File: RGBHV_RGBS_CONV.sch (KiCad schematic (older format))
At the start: 29 parts, among them J1 DIGITAL RGB, J10 ENABLE_DIVIDE, J11 RGBHV_1, J12 LOGIC_SINGLE, J13 LOGIC_DOUBLE, J14 ENABLE_MARGE, J15 RGBS_OUT, J16 RGBS_OUT, J17 +5V IN, J18 +5V OUT, J2 VGA DB15, J3 ANALOG RGB DB15, J4 X1, J5 DIGITAL_RGBHV_1, J6 ANALOG RGB, J7 DIGITAL_RGBHV_2, J8 ANALOG RGB VGA, J9 RGBHV_1, U1 LM1881, U2 74HC86

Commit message: Rev.5A DIn8 fix and remove sync sep.
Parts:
- removed C1: C, Capacitors_ThroughHole:C_Disc_D4.3mm_W1.9mm_P5.00mm, symbol Device:C
- removed C3, C4: C, Capacitors_ThroughHole:C_Disc_D4.3mm_W1.9mm_P5.00mm, symbol device:C
- removed J10: ENABLE_DIVIDE, Pin_Headers:Pin_Header_Straight_1x02_Pitch2.54mm, symbol Connector_Generic:Conn_01x02
- removed J12: LOGIC_SINGLE, Pin_Headers:Pin_Header_Straight_1x02_Pitch2.54mm, symbol Connector_Generic:Conn_01x02
- removed J13: LOGIC_DOUBLE, Pin_Headers:Pin_Header_Straight_1x02_Pitch2.54mm, symbol Connector_Generic:Conn_01x02
- removed J14: ENABLE_MARGE, Pin_Headers:Pin_Header_Straight_1x02_Pitch2.54mm, symbol Connector_Generic:Conn_01x02
- removed J8: ANALOG RGB VGA, Pin_Headers:Pin_Header_Straight_2x08_Pitch2.54mm, symbol Connector_Generic:Conn_02x08_Top_Bottom
- removed R4: R, Resistors_ThroughHole:R_Axial_DIN0204_L3.6mm_D1.6mm_P5.08mm_Horizontal, symbol Device:R
- removed RV1: R_POT, Potentiometers:Potentiometer_Triwood_RM-065, symbol Device:R_POT
- removed U1: LM1881, Housings_DIP:DIP-8_W7.62mm, symbol Video:LM1881
- removed U2: 74HC86, Housings_DIP:DIP-14_W7.62mm, symbol ryuk_org:74HC86
- added J8: ANALOG RGB DA15 EDGE, ryuk_lib:D-SUB15_PCB_EDGE, symbol Connector:DB15_Female_MountingHoles
- added U2: 4070/74HC86, symbol ryuk_lib:74HC86-ryuk_org-RGBHV_RGBS_CONV-rescue-RGBHV_RGBS_CONV-rescue
- J3: value ANALOG RGB DB15 -> ANALOG RGB DA15
- R1, R2, R3: footprint Resistors_ThroughHole:R_Axial_DIN0204_L3.6mm_D1.6mm_P5.08mm_Horizontal -> Resistor_THT:R_Axial_DIN0204_L3.6mm_D1.6mm_P7.62mm_Horizontal
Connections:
- wire segments 172 -> 138
- no-connect marks 44 -> 49
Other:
- moved on the sheet: C2, J1, J11, J15, J16, J17, J18, J2, J3, J4, J5, J6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

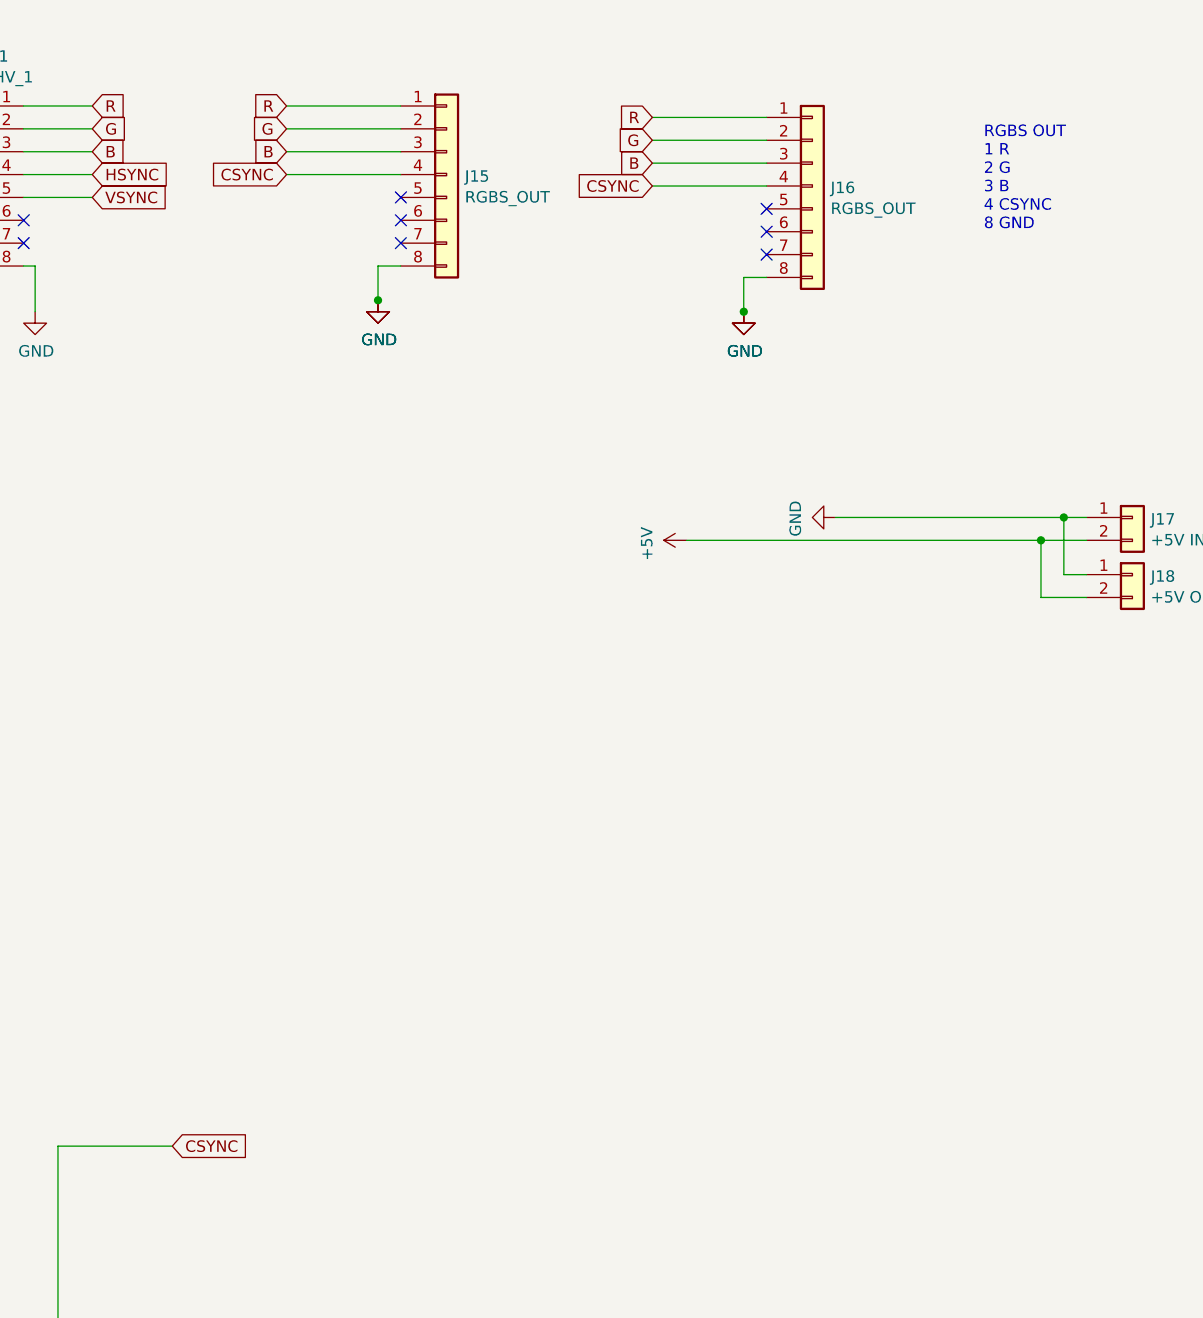
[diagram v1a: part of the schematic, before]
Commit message: Rev.5B Add RGBS VR
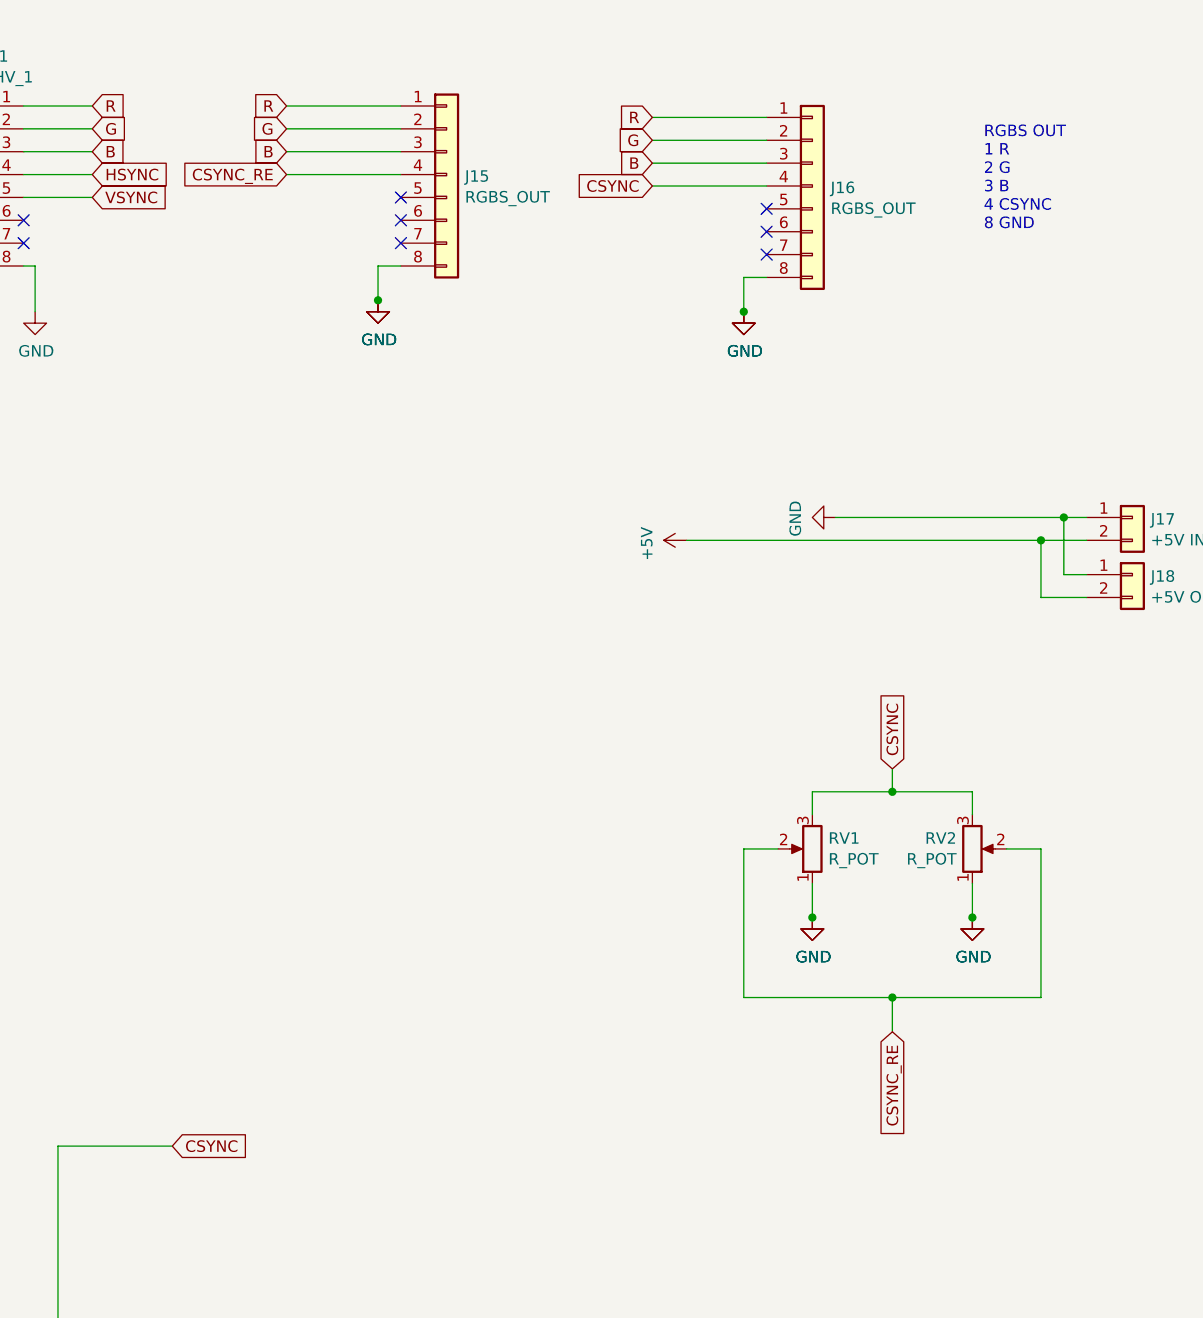
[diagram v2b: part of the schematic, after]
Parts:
- added RV1, RV2: R_POT, Potentiometer_THT:Potentiometer_Bourns_3296W_Vertical, symbol Device:R_POT
- U2: footprint (none) -> Package_DIP:DIP-14_W7.62mm
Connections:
- net CSYNC: now also RV1.3, RV2.3; no longer J15.4 (Pin_4)
- net GND: now also RV1.1, RV2.1
- new net CSYNC_RE: J15.4 (Pin_4), RV1.2, RV2.2
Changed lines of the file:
@@
 	14250 3550 15250 3550
 Text GLabel 11850 2050 0    50   Input ~ 0
-CSYNC
+CSYNC_RE
 $Comp
 L power:GND #PWR026
@@
 Wire Wire Line
 	2050 5150 2950 5150
+NoConn ~ 6700 2250
+NoConn ~ 6700 2350
+NoConn ~ 9750 2250
+NoConn ~ 9750 2350
+NoConn ~ 10700 2250
+NoConn ~ 10700 2350
+Wire Wire Line
+	10850 6300 10850 8200
+Wire Wire Line
+	9700 8200 10850 8200
+Wire Wire Line
+	10150 8400 12050 8400
+$Comp
+L power:GND #PWR012
+U 1 1 5D43FAA1
+P 6100 5650
+F 0 "#PWR012" H 6100 5400 50  0001 C CNN
+F 1 "GND" H 6105 5477 50  0000 C CNN
+F 2 "" H 6100 5650 50  0001 C CNN
+F 3 "" H 6100 5650 50  0001 C CNN
+	1    6100 5650
+	1    0    0    -1
+$EndComp
+Wire Wire Line
+	6100 5450 6100 5650
+Wire Wire Line
+	5800 3850 5050 3850
+Wire Wire Line
+	4950 4250 5800 4250
+Wire Wire Line
+	5800 4650 4850 4650
+Wire Wire Line
+	5800 4050 5400 4050
+Wire Wire Line
+	5400 4050 5400 4450
+Wire Wire Line
+	5400 4450 5800 4450
+Wire Wire Line
+	5400 4850 5800 4850
+Connection ~ 5400 4450
+Connection ~ 5400 4850
+$Comp
+L power:GND #PWR010
+U 1 1 5D43FAB5
+P 5400 5450
+F 0 "#PWR010" H 5400 5200 50  0001 C CNN
+F 1 "GND" H 5405 5277 50  0000 C CNN
+F 2 "" H 5400 5450 50  0001 C CNN
+F 3 "" H 5400 5450 50  0001 C CNN
+	1    5400 5450
+	1    0    0    -1
+$EndComp
+NoConn ~ 5800 3950
+NoConn ~ 5800 4150
+NoConn ~ 5800 4350
+NoConn ~ 5800 4750
+NoConn ~ 5800 5050
+Wire Wire Line
+	5400 4850 5400 5450
+NoConn ~ 5800 5250
+Wire Wire Line
+	5400 4450 5400 4850
+NoConn ~ 5800 4550
+Text GLabel 4900 4950 0    50   Input ~ 0
+HSYNC
+Text GLabel 4900 5150 0    50   Input ~ 0
+VSYNC
+Text GLabel 4950 4250 0    50   Input ~ 0
+G
+Text GLabel 5050 3850 0    50   Input ~ 0
+R
+Text GLabel 4850 4650 0    50   Input ~ 0
+B
+Wire Wire Line
+	4900 4950 5800 4950
+Wire Wire Line
+	4900 5150 5800 5150
+$Comp
+L Connector:DB15_Female_MountingHoles J8
+U 1 1 5D43FA97
+P 6100 4550
+F 0 "J8" H 6255 4553 50  0000 L CNN
+F 1 "ANALOG RGB DA15 EDGE" H 6255 4462 50  0000 L CNN
+F 2 "ryuk_lib:D-SUB15_PCB_EDGE" H 6100 4550 50  0001 C CNN
+F 3 " ~" H 6100 4550 50  0001 C CNN
+	1    6100 4550
+	1    0    0    -1
+$EndComp
+$Comp
+L ryuk_lib:74HC86-ryuk_org-RGBHV_RGBS_CONV-rescue-RGBHV_RGBS_CONV-rescue U2
+U 1 1 5D6710B5
+P 10150 7400
+F 0 "U2" V 10104 7428 50  0000 L CNN
+F 1 "4070/74HC86" V 10195 7428 50  0000 L CNN
+F 2 "Package_DIP:DIP-14_W7.62mm" H 10150 7400 50  0001 C CNN
+F 3 "" H 10150 7400 50  0001 C CNN
+	1    10150 7400
+	0    1    1    0
+$EndComp
+Wire Wire Line
+	13450 2100 13950 2100
+Connection ~ 13850 2650
+Wire Wire Line
+	13450 2000 13950 2000
+Wire Wire Line
+	13450 1900 13950 1900
+Wire Wire Line
+	13450 1800 13950 1800
+$Comp
+L power:GND #PWR024
+U 1 1 5CF92D5E
+P 13850 2650
+F 0 "#PWR024" H 13850 2400 50  0001 C CNN
+F 1 "GND" H 13855 2477 50  0000 C CNN
+F 2 "" H 13850 2650 50  0001 C CNN
+F 3 "" H 13850 2650 50  0001 C CNN
+	1    13850 2650
+	1    0    0    -1
+$EndComp
+$Comp
+L Connector_Generic:Conn_01x08 J16
+U 1 1 5CF92D58
+P 14150 2100
+F 0 "J16" H 14230 2092 50  0000 L CNN
+F 1 "RGBS_OUT" H 14230 2001 50  0000 L CNN
+F 2 "Pin_Headers:Pin_Header_Straight_1x08_Pitch2.54mm" H 14150 2100 50  0001 C CNN
+F 3 "~" H 14150 2100 50  0001 C CNN
+	1    14150 2100
+	1    0    0    -1
+$EndComp
+Text GLabel 13450 2000 0    50   Input ~ 0
+B
+Text GLabel 13450 1800 0    50   Input ~ 0
+R
+Text GLabel 13450 1900 0    50   Input ~ 0
+G
+Text GLabel 13450 2100 0    50   Input ~ 0
+CSYNC
+NoConn ~ 13950 2200
+NoConn ~ 13950 2300
+NoConn ~ 13950 2400
+Wire Wire Line
+	13850 2500 13850 2650
+Wire Wire Line
+	13950 2500 13850 2500
 $Comp
 L power:GND #PWR023
@@
 	1    0    0    -1
 $EndComp
-Wire Wire Line
-	13950 2500 13850 2500
-Wire Wire Line
-	13850 2500 13850 2650
-NoConn ~ 13950 2400
-NoConn ~ 13950 2300
-NoConn ~ 13950 2200
-Text GLabel 13450 2100 0    50   Input ~ 0
+$Comp
+L Device:R_POT RV2
+U 1 1 5E243AED
+P 14850 5000
+F 0 "RV2" H 14781 4954 50  0000 R CNN
+F 1 "R_POT" H 14781 5045 50  0000 R CNN
+F 2 "Potentiometer_THT:Potentiometer_Bourns_3296W_Vertical" H 14850 5000 50  0001 C CNN
+F 3 "~" H 14850 5000 50  0001 C CNN
+	1    14850 5000
+	1    0    0    1
+$EndComp
+$Comp
+L Device:R_POT RV1
+U 1 1 5E2442D3
+P 14150 5000
+F 0 "RV1" H 14080 4954 50  0000 R CNN
+F 1 "R_POT" H 14080 5045 50  0000 R CNN
+F 2 "Potentiometer_THT:Potentiometer_Bourns_3296W_Vertical" H 14150 5000 50  0001 C CNN
+F 3 "~" H 14150 5000 50  0001 C CNN
+	1    14150 5000
+	-1   0    0    1
+$EndComp
+$Comp
+L power:GND #PWR0101
+U 1 1 5E24B2D8
+P 14150 5300
+F 0 "#PWR0101" H 14150 5050 50  0001 C CNN
+F 1 "GND" H 14155 5127 50  0000 C CNN
+F 2 "" H 14150 5300 50  0001 C CNN
+F 3 "" H 14150 5300 50  0001 C CNN
+	1    14150 5300
+	1    0    0    -1
+$EndComp
+Wire Wire Line
+	14150 5150 14150 5300
+$Comp
+L power:GND #PWR0102
+U 1 1 5E24B2E3
+P 14150 5300
+F 0 "#PWR0102" H 14150 5050 50  0001 C CNN
+F 1 "GND" H 14155 5127 50  0000 C CNN
+F 2 "" H 14150 5300 50  0001 C CNN
+F 3 "" H 14150 5300 50  0001 C CNN
+	1    14150 5300
+	1    0    0    -1
+$EndComp
+$Comp
+L power:GND #PWR0103
+U 1 1 5E25311B
+P 14850 5300
+F 0 "#PWR0103" H 14850 5050 50  0001 C CNN
+F 1 "GND" H 14855 5127 50  0000 C CNN
+F 2 "" H 14850 5300 50  0001 C CNN
+F 3 "" H 14850 5300 50  0001 C CNN
+	1    14850 5300
+	1    0    0    -1
+$EndComp
+Wire Wire Line
+	14850 5150 14850 5300
+$Comp
+L power:GND #PWR0104
+U 1 1 5E253126
+P 14850 5300
+F 0 "#PWR0104" H 14850 5050 50  0001 C CNN
+F 1 "GND" H 14855 5127 50  0000 C CNN
+F 2 "" H 14850 5300 50  0001 C CNN
+F 3 "" H 14850 5300 50  0001 C CNN
+	1    14850 5300
+	1    0    0    -1
+$EndComp
+Wire Wire Line
+	14000 5000 13850 5000
+Wire Wire Line
+	13850 5000 13850 5650
+Wire Wire Line
+	13850 5650 14500 5650
+Wire Wire Line
+	15150 5650 15150 5000
+Wire Wire Line
+	15150 5000 15000 5000
+Wire Wire Line
+	14500 5650 14500 5800
+Connection ~ 14500 5650
+Wire Wire Line
+	14500 5650 15150 5650
+Wire Wire Line
+	14850 4850 14850 4750
+Wire Wire Line
+	14850 4750 14500 4750
+Wire Wire Line
+	14150 4750 14150 4850
+Wire Wire Line
+	14500 4750 14500 4650
+Connection ~ 14500 4750
+Wire Wire Line
+	14500 4750 14150 4750
+Connection ~ 14850 5300
+Text GLabel 14500 4650 1    50   Input ~ 0
 CSYNC
-Text GLabel 13450 1900 0    50   Input ~ 0
-G
-Text GLabel 13450 1800 0    50   Input ~ 0
-R
-Text GLabel 13450 2000 0    50   Input ~ 0
-B
-$Comp
-L Connector_Generic:Conn_01x08 J16
-U 1 1 5CF92D58
-P 14150 2100
-F 0 "J16" H 14230 2092 50  0000 L CNN
-F 1 "RGBS_OUT" H 14230 2001 50  0000 L CNN
-F 2 "Pin_Headers:Pin_Header_Straight_1x08_Pitch2.54mm" H 14150 2100 50  0001 C CNN
-F 3 "~" H 14150 2100 50  0001 C CNN
-	1    14150 2100
-	1    0    0    -1
-$EndComp
-$Comp
-L power:GND #PWR024
-U 1 1 5CF92D5E
-P 13850 2650
-F 0 "#PWR024" H 13850 2400 50  0001 C CNN
-F 1 "GND" H 13855 2477 50  0000 C CNN
-F 2 "" H 13850 2650 50  0001 C CNN
-F 3 "" H 13850 2650 50  0001 C CNN
-	1    13850 2650
-	1    0    0    -1
-$EndComp
-Wire Wire Line
-	13450 1800 13950 1800
-Wire Wire Line
-	13450 1900 13950 1900
-Wire Wire Line
-	13450 2000 13950 2000
-Connection ~ 13850 2650
-Wire Wire Line
-	13450 2100 13950 2100
-NoConn ~ 6700 2250
-NoConn ~ 6700 2350
-NoConn ~ 9750 2250
-NoConn ~ 9750 2350
-NoConn ~ 10700 2250
-NoConn ~ 10700 2350
-Wire Wire Line
-	10850 6300 10850 8200
-Wire Wire Line
-	9700 8200 10850 8200
-Wire Wire Line
-	10150 8400 12050 8400
-$Comp
-L power:GND #PWR012
-U 1 1 5D43FAA1
-P 6100 5650
-F 0 "#PWR012" H 6100 5400 50  0001 C CNN
-F 1 "GND" H 6105 5477 50  0000 C CNN
-F 2 "" H 6100 5650 50  0001 C CNN
-F 3 "" H 6100 5650 50  0001 C CNN
-	1    6100 5650
-	1    0    0    -1
-$EndComp
-Wire Wire Line
-	6100 5450 6100 5650
-Wire Wire Line
-	5800 3850 5050 3850
-Wire Wire Line
-	4950 4250 5800 4250
-Wire Wire Line
-	5800 4650 4850 4650
-Wire Wire Line
-	5800 4050 5400 4050
-Wire Wire Line
-	5400 4050 5400 4450
-Wire Wire Line
-	5400 4450 5800 4450
-Wire Wire Line
-	5400 4850 5800 4850
-Connection ~ 5400 4450
-Connection ~ 5400 4850
-$Comp
-L power:GND #PWR010
-U 1 1 5D43FAB5
-P 5400 5450
-F 0 "#PWR010" H 5400 5200 50  0001 C CNN
-F 1 "GND" H 5405 5277 50  0000 C CNN
-F 2 "" H 5400 5450 50  0001 C CNN
-F 3 "" H 5400 5450 50  0001 C CNN
-	1    5400 5450
-	1    0    0    -1
-$EndComp
-NoConn ~ 5800 3950
-NoConn ~ 5800 4150
-NoConn ~ 5800 4350
-NoConn ~ 5800 4750
-NoConn ~ 5800 5050
-Wire Wire Line
-	5400 4850 5400 5450
-NoConn ~ 5800 5250
-Wire Wire Line
-	5400 4450 5400 4850
-NoConn ~ 5800 4550
-Text GLabel 4900 4950 0    50   Input ~ 0
-HSYNC
-Text GLabel 4900 5150 0    50   Input ~ 0
-VSYNC
-Text GLabel 4950 4250 0    50   Input ~ 0
-G
-Text GLabel 5050 3850 0    50   Input ~ 0
-R
-Text GLabel 4850 4650 0    50   Input ~ 0
-B
-Wire Wire Line
-	4900 4950 5800 4950
-Wire Wire Line
-	4900 5150 5800 5150
-$Comp
-L Connector:DB15_Female_MountingHoles J8
-U 1 1 5D43FA97
-P 6100 4550
-F 0 "J8" H 6255 4553 50  0000 L CNN
-F 1 "ANALOG RGB DA15 EDGE" H 6255 4462 50  0000 L CNN
-F 2 "ryuk_lib:D-SUB15_PCB_EDGE" H 6100 4550 50  0001 C CNN
-F 3 " ~" H 6100 4550 50  0001 C CNN
-	1    6100 4550
-	1    0    0    -1
-$EndComp
-$Comp
-L ryuk_lib:74HC86-ryuk_org-RGBHV_RGBS_CONV-rescue-RGBHV_RGBS_CONV-rescue U2
-U 1 1 5D6710B5
-P 10150 7400
-F 0 "U2" V 10104 7428 50  0000 L CNN
-F 1 "4070/74HC86" V 10195 7428 50  0000 L CNN
-F 2 "" H 10150 7400 50  0001 C CNN
-F 3 "" H 10150 7400 50  0001 C CNN
-	1    10150 7400
-	0    1    1    0
-$EndComp
+Text GLabel 14500 5800 3    50   Input ~ 0
+CSYNC_RE
+Connection ~ 14150 5300
 $EndSCHEMATC

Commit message: Rev1.0B
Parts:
- removed C2: C, Capacitors_ThroughHole:C_Disc_D4.3mm_W1.9mm_P5.00mm, symbol Device:C
- removed J18: +5V OUT, Pin_Headers:Pin_Header_Straight_1x02_Pitch2.54mm, symbol Connector_Generic:Conn_01x02
- removed J8: ANALOG RGB DA15 EDGE, ryuk_lib:D-SUB15_PCB_EDGE, symbol Connector:DB15_Female_MountingHoles
- removed RV1, RV2: R_POT, Potentiometer_THT:Potentiometer_Bourns_3296W_Vertical, symbol Device:R_POT
- added C1, C4, C6: 0.1uF, Capacitor_THT:C_Disc_D5.0mm_W2.5mm_P5.00mm, symbol Device:C
- added C3, C5: 10uF, Capacitor_THT:C_Disc_D5.0mm_W2.5mm_P5.00mm, symbol Device:C
- added H1, H2, H3, H4: M4, MountingHole:MountingHole_4.3mm_M4_Pad, symbol Mechanical:MountingHole_Pad
- added J10: AUDIO1, ryuk_lib:PJ-3900-04, symbol Connector:AudioJack3
- added J12: AUDIO2, ryuk_lib:PJ-3900-04, symbol Connector:AudioJack3
- added J8: SWITCHER, Connector_IDC:IDC-Header_2x05_P2.54mm_Vertical, symbol Connector_Generic:Conn_01x10
- added R10, R4, R7: 0R-NO_LOAD, Resistor_THT:R_Axial_DIN0207_L6.3mm_D2.5mm_P10.16mm_Horizontal, symbol Device:R
- added R11: 100R-NO_LOAD, Resistor_THT:R_Axial_DIN0207_L6.3mm_D2.5mm_P10.16mm_Horizontal, symbol Device:R
- added R5, R6, R9: 150R, Resistor_THT:R_Axial_DIN0207_L6.3mm_D2.5mm_P10.16mm_Horizontal, symbol Device:R
- added R8: 10KR, Resistor_THT:R_Axial_DIN0207_L6.3mm_D2.5mm_P10.16mm_Horizontal, symbol Device:R
- added U1: OUT_GND_IN_3.3V, Package_TO_SOT_THT:TO-220-3_Vertical, symbol Regulator_Linear:LM7805_TO220
- added U3: OUT_IN_GND_3.3V, Package_TO_SOT_THT:TO-220-3_Vertical, symbol Regulator_Linear:HT75xx-1-SOT89
- J1: footprint ryuk_org_lib:DIN 8 PCB -> ryuk_lib:DIN 8 PCB
- J11: value RGBHV_1 -> RGBHV_2; footprint Pin_Headers:Pin_Header_Straight_1x08_Pitch2.54mm -> Connector_JST:JST_XH_B8B-XH-A_1x08_P2.50mm_Vertical
- J15: value RGBS_OUT -> RGBS_OUT1; footprint Pin_Headers:Pin_Header_Straight_1x08_Pitch2.54mm -> Connector_JST:JST_XH_B8B-XH-A_1x08_P2.50mm_Vertical
- J16: value RGBS_OUT -> RGBS_OUT2; footprint Pin_Headers:Pin_Header_Straight_1x08_Pitch2.54mm -> Connector_JST:JST_XH_S8B-XH-A_1x08_P2.50mm_Horizontal
- J17: value +5V IN -> VIN; footprint Pin_Headers:Pin_Header_Straight_1x02_Pitch2.54mm -> Connector_JST:JST_XH_S2B-XH-A_1x02_P2.50mm_Horizontal
- J2: footprint ryuk_org_lib:DB_15F-VGA_L -> ryuk_lib:DB_15F-VGA_L
- J3: footprint w_conn_d-sub:DB_15F -> Connector_Dsub:DSUB-15_Female_Horizontal_P2.77x2.84mm_EdgePinOffset4.94mm_Housed_MountingHolesOffset7.48mm
- J4: footprint ryuk_org_lib:DIN 6 PCB SDS-60J -> ryuk_lib:DIN_6_PCB
- J5, J7, J9: footprint Pin_Headers:Pin_Header_Straight_1x08_Pitch2.54mm -> Connector_JST:JST_XH_B8B-XH-A_1x08_P2.50mm_Vertical
- J6: footprint Pin_Headers:Pin_Header_Straight_2x08_Pitch2.54mm -> Connector_IDC:IDC-Header_2x08_P2.54mm_Vertical
- R1, R2, R3: footprint Resistor_THT:R_Axial_DIN0204_L3.6mm_D1.6mm_P7.62mm_Horizontal -> Resistor_THT:R_Axial_DIN0207_L6.3mm_D2.5mm_P10.16mm_Horizontal
- U2: value 4070/74HC86 -> 74HC86
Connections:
- net CSYNC_RE is gone; now on net CSYNC: J15.4 (Pin_4)
- net B: now also J8.3 (Pin_3)
- net CSYNC: now also R10.2, R11.2, R9.2; no longer U2.11 (Y4)
- net G: now also J8.2 (Pin_2)
- net GND: now also J3.12 (P12), J3.8, J6.15 (Pin_15), J6.8 (Pin_8), U2.10 (B3), U2.4 (A2), U2.5 (B2), U2.9 (A3), C1.1, C3.2, C4.2, C5.2, C6.2, H1.1, H2.1, H3.1, H4.1, J10.S, J12.S, J8.10 (Pin_10), J8.6 (Pin_6), J8.9 (Pin_9), R11.1, U1.2 (GND), U3.1 (GND)
- net HSYNC: now also J8.4 (Pin_4), R6.1, R7.1; no longer U2.2 (B1)
- net R: now also J8.1 (Pin_1)
- net VSYNC: now also J15.5 (Pin_5), J16.5 (Pin_5), J8.5 (Pin_5), R4.1, R5.1; no longer U2.1 (A1)
- net AUDIO_L: now reaches J7.6 (Pin_6)
- net AUDIO_L: now also J11.6 (Pin_6), J15.6 (Pin_6), J16.6 (Pin_6), J3.10 (P10), J5.6 (Pin_6), J6.4 (Pin_4), J9.6 (Pin_6), J10.T, J12.T, J8.7 (Pin_7)
- net AUDIO_R: now reaches J7.7 (Pin_7)
- net AUDIO_R: now also J11.7 (Pin_7), J15.7 (Pin_7), J16.7 (Pin_7), J3.11 (P111), J5.7 (Pin_7), J6.6 (Pin_6), J9.7 (Pin_7), J10.R, J12.R, J8.8 (Pin_8)
- net at U2.13 (B4): now also R8.1; no longer U2.3 (Y1)
- removed net +5V: J17.2 (Pin_2), U2.12 (A4), U2.14 (VCC)
- new net: C3.1, C4.1, J17.2 (Pin_2), U1.1 (VI), U3.2 (VIN)
- new net: R4.2, R5.2, U2.1 (A1)
- new net: R10.1, R9.1, U2.11 (Y4)
- new net: U2.12 (A4), U2.3 (Y1)
- new net: R6.2, R7.2, U2.2 (B1)
- new net +3V3: C1.2, C5.1, C6.1, R8.2, U1.3 (VO), U2.14 (VCC), U3.3 (VOUT)
- no-connect marks 49 -> 16
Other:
- note added: "ANAROG RGB CONN\n1(1) R\n5(3) G\n9(5) B\n3.7.8.11.15(2.4.6.8.12) GND\n4(10) AUDIO L\n6(11) AUDIO R\n12(14) HSYNC\n14(15) VSYNC"
- note added: "RGBHV OUT\n1 R\n2 G\n3 B\n4 HSYNC\n5 VSYNC\n6 AUDIO_R\n7 AUDIO_L\n8 GND"
- note removed: "ANAROG RGB CONN\n1(1) R\n5(3) G\n9(5) B\n3.7.8.11.15(2.4.6.8.12) GND\n12(14) HSYNC\n14(15) VSYNC"
- note removed: "RGBHV OUT\n1 R\n2 G\n3 B\n4 HSYNC\n5 VSYNC\n6 NC\n7 NC\n8 GND"
- moved on the sheet: J11, J17, J6
